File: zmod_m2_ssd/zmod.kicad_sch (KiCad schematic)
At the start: 22 parts, among them J1 MDT420M02001, J2 QTH-020-01-X-D-DP-A, U1 SN74LVC1T45DBV, U2 LTC6957xMS-2, X1 ECS-2520MVQ-1000-BN-TR

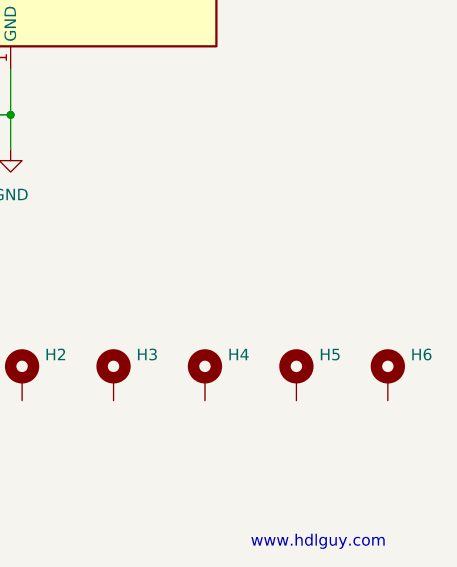
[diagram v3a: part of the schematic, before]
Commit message: added mounting hole for M.2 screw
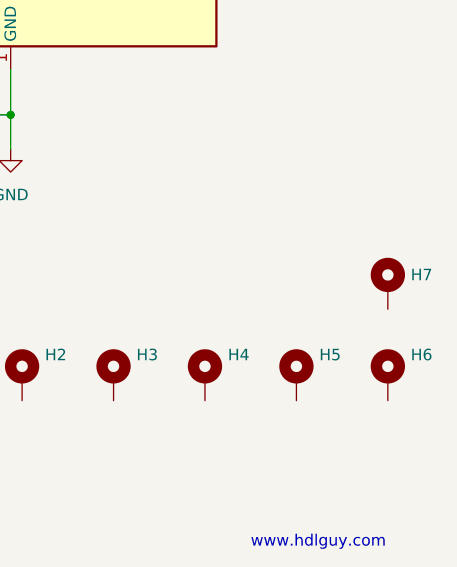
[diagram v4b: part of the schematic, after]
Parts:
- added H7: MountingHole_Pad, MountingHole:MountingHole_2.7mm_Pad, symbol Mechanical:MountingHole_Pad
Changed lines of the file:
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@@
+    (pin "1")
+  )
+  (symbol (lib_id "Mechanical:MountingHole_Pad") (at 279.4 151.13 0) (unit 1)
+    (in_bom yes) (on_board yes) (fields_autoplaced)
+    (property "Reference" "H7" (id 0) (at 281.94 149.8599 0)
+      (effects (font (size 1.27 1.27)) (justify left))
+    )
+    (property "Value" "MountingHole_Pad" (id 1) (at 281.94 151.1299 0)
+      (effects (font (size 1.27 1.27)) (justify left) hide)
+    )
+    (property "Footprint" "MountingHole:MountingHole_2.7mm_Pad" (id 2) (at 279.4 151.13 0)
+      (effects (font (size 1.27 1.27)) hide)
+    )
+    (property "Datasheet" "~" (id 3) (at 279.4 151.13 0)
+      (effects (font (size 1.27 1.27)) hide)
+    )
     (pin "1")
   )
@@
       (reference "H6") (unit 1) (value "MountingHole_Pad") (footprint "MountingHole:MountingHole_3.2mm_M3_DIN965_Pad_TopBottom")
     )
+    (path "/5216a05f-00bb-4954-a8d0-d0c5066122b7"
+      (reference "H7") (unit 1) (value "MountingHole_Pad") (footprint "MountingHole:MountingHole_2.7mm_Pad")
+    )
     (path "/713a8cb6-be5c-413a-968b-156735b7e9f4"

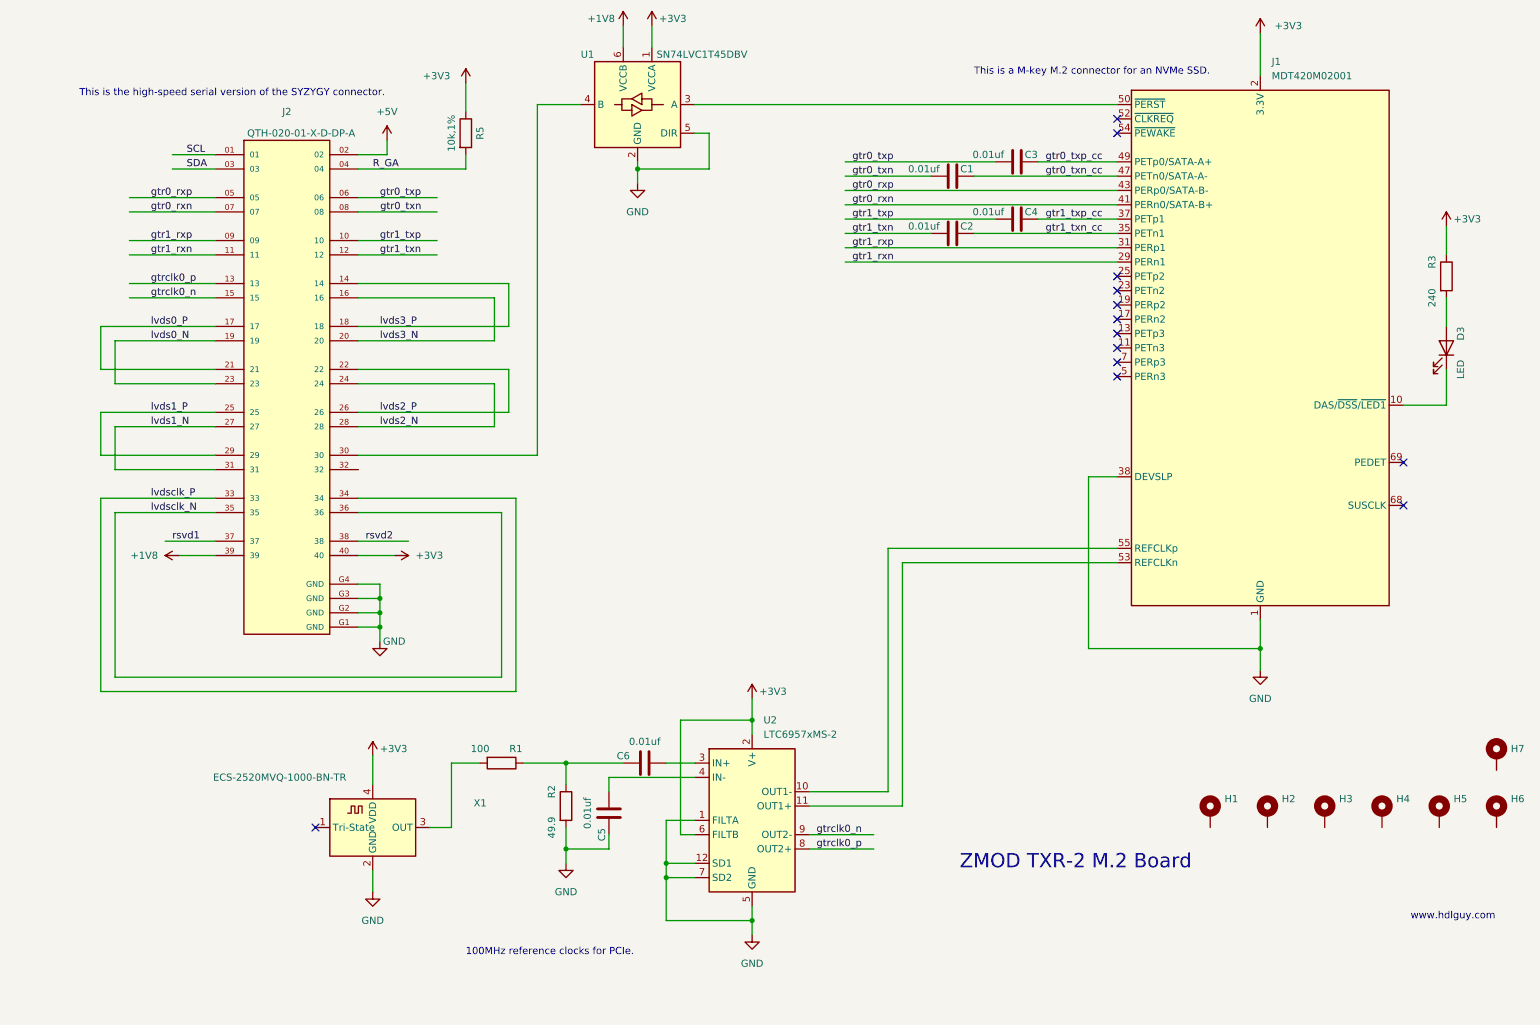
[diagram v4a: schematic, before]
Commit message: first cut at routing the m.2 zmod
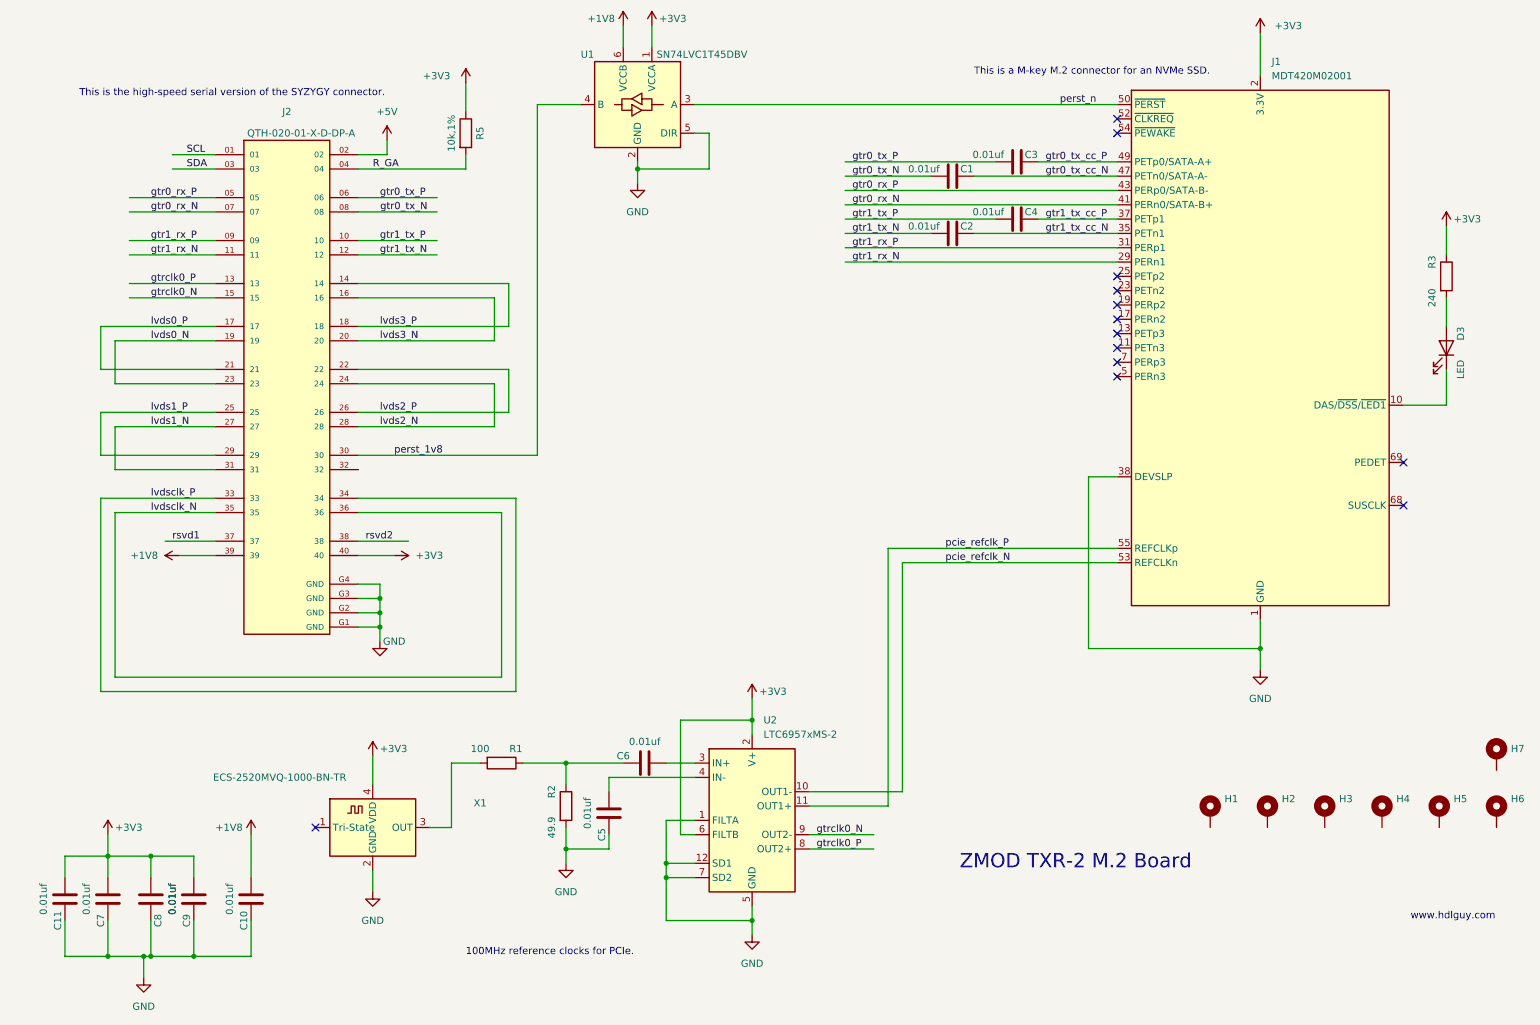
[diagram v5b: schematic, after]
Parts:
- added C10, C11, C7, C8, C9: 0.01uf, Capacitor_SMD:C_0603_1608Metric, symbol Device:C
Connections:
- net +1V8: now also C10.2
- net +3V3: now also C11.2, C7.2, C8.2, C9.2
- net GND: now also C10.1, C11.1, C7.1, C8.1, C9.1
- net perst_1v8: now reaches J2.30, U1.4 (B)
- net perst_n: now reaches J1.50 (~{PERST}), U1.3 (A)
- net pcie_refclk_N: now reaches J1.53 (REFCLKn)
- net pcie_refclk_N: now also U2.10 (OUT1-); no longer U2.11 (OUT1+)
- net pcie_refclk_P: now reaches J1.55 (REFCLKp)
- net pcie_refclk_P: now also U2.11 (OUT1+); no longer U2.10 (OUT1-)
- net gtr0_rxn renamed gtr0_rx_N
- net gtr0_rxp renamed gtr0_rx_P
- net gtr0_txn renamed gtr0_tx_N
- net gtr0_txn_cc renamed gtr0_tx_cc_N
- net gtr0_txp renamed gtr0_tx_P
- net gtr0_txp_cc renamed gtr0_tx_cc_P
- net gtr1_rxn renamed gtr1_rx_N
- net gtr1_rxp renamed gtr1_rx_P
- net gtr1_txn renamed gtr1_tx_N
- net gtr1_txn_cc renamed gtr1_tx_cc_N
- net gtr1_txp renamed gtr1_tx_P
- net gtr1_txp_cc renamed gtr1_tx_cc_P
- net gtrclk0_n renamed gtrclk0_N
- net gtrclk0_p renamed gtrclk0_P

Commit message: ready to send to Oshpark
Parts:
- removed R5: 10k,1%, Resistor_SMD:R_0603_1608Metric, symbol Device:R
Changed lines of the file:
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@@
-    (stroke (width 0) (type default) (color 0 0 0 0))
-  )
-  (wire (pts (xy 96.52 44.45) (xy 96.52 46.99))
     (stroke (width 0) (type default) (color 0 0 0 0))
   )
@@
   )
   (wire (pts (xy 43.18 113.03) (xy 52.07 113.03))
-    (stroke (width 0) (type default) (color 0 0 0 0))
-  )
-  (wire (pts (xy 96.52 31.75) (xy 96.52 36.83))
     (stroke (width 0) (type default) (color 0 0 0 0))
   )
@@
     (pin "1")
     (pin "2")
-  )
-  (symbol (lib_id "power:+3V3") (at 96.52 31.75 0) (unit 1)
-    (in_bom yes) (on_board yes)
-    (property "Reference" "#PWR03" (id 0) (at 96.52 35.56 0)
-      (effects (font (size 1.27 1.27)) hide)
-    )
-    (property "Value" "+3V3" (id 1) (at 88.9 30.48 0)
-      (effects (font (size 1.27 1.27)) (justify left))
-    )
-    (property "Footprint" "" (id 2) (at 96.52 31.75 0)
-      (effects (font (size 1.27 1.27)) hide)
-    )
-    (property "Datasheet" "" (id 3) (at 96.52 31.75 0)
-      (effects (font (size 1.27 1.27)) hide)
-    )
-    (pin "1")
   )
   (symbol (lib_id "Device:R") (at 270.51 66.04 0) (unit 1)
@@
     (pin "2")
   )
-  (symbol (lib_id "Device:R") (at 96.52 40.64 0) (unit 1)
-    (in_bom yes) (on_board yes)
-    (property "Reference" "R5" (id 0) (at 99.06 40.64 90))
-    (property "Value" "10k,1%" (id 1) (at 93.98 40.64 90))
-    (property "Footprint" "Resistor_SMD:R_0603_1608Metric" (id 2) (at 94.742 40.64 90)
-      (effects (font (size 1.27 1.27)) hide)
-    )
-    (property "Datasheet" "~" (id 3) (at 96.52 40.64 0)
-      (effects (font (size 1.27 1.27)) hide)
-    )
-    (pin "1")
-    (pin "2")
-  )
   (symbol (lib_id "Device:C") (at 194.31 45.72 90) (unit 1)
     (in_bom yes) (on_board yes)
@@
       (reference "#PWR02") (unit 1) (value "+5V") (footprint "")
     )
-    (path "/31cfe908-0bdc-41ed-bcd3-98cd266b0e0c"
-      (reference "#PWR03") (unit 1) (value "+3V3") (footprint "")
-    )
     (path "/bc364ec4-e3bc-4253-a49e-0029f83e8206"
       (reference "#PWR04") (unit 1) (value "+3V3") (footprint "")
@@
       (reference "R3") (unit 1) (value "240") (footprint "Resistor_SMD:R_0603_1608Metric")
     )
-    (path "/dfac8798-32e6-44ce-82d4-45466d68831c"
-      (reference "R5") (unit 1) (value "10k,1%") (footprint "Resistor_SMD:R_0603_1608Metric")
-    )
     (path "/87fac8eb-3e82-4d31-b181-231059959fd9"

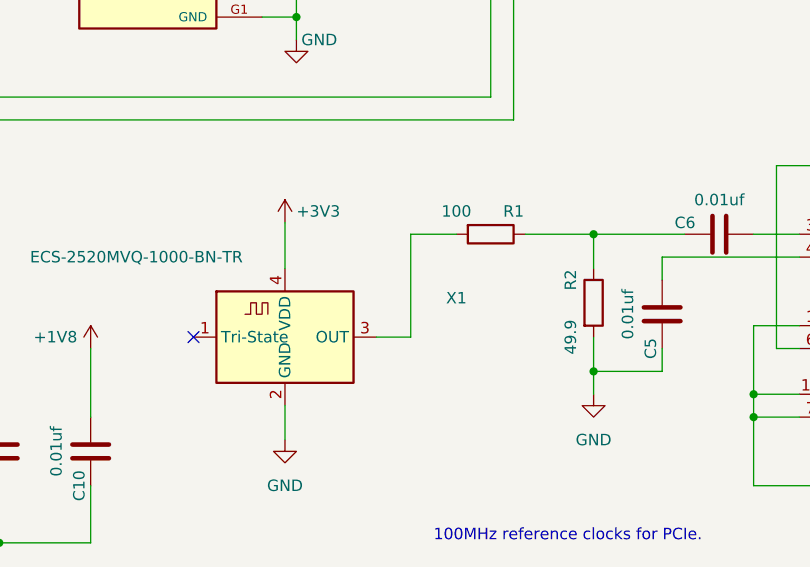
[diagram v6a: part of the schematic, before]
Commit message: updated oscilltor symbol and footprint to have 3D model
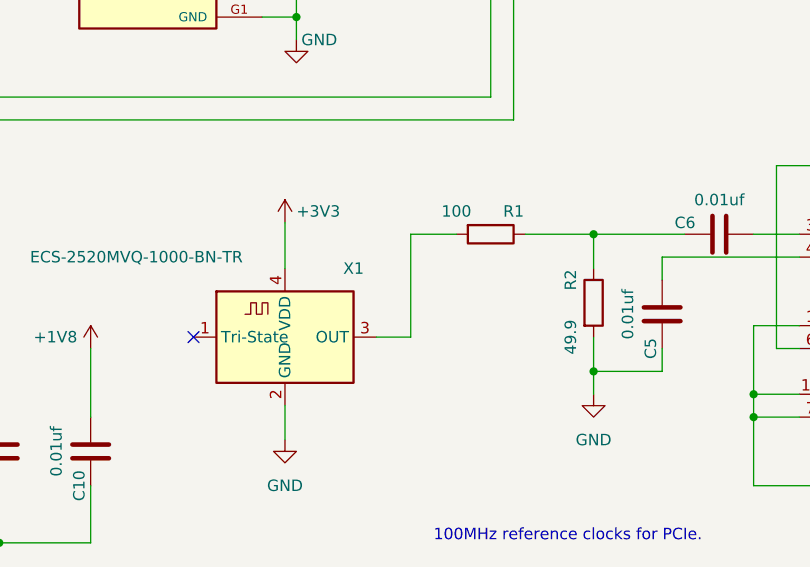
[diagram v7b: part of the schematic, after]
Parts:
- X1: footprint Oscillator:Oscillator_SMD_ECS_2520MV-xxx-xx-4Pin_2.5x2.0mm -> pedrolib:OSC_ECS-2520S25-250-FN-TR; symbol Oscillator:ECS-2520MV-xxx-xx -> pedrolib:ECS-2520MV-xxx-xx
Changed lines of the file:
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@@
     (pin "1")
   )
-  (symbol (lib_id "Oscillator:ECS-2520MV-xxx-xx") (at 80.01 163.83 0) (unit 1)
-    (in_bom yes) (on_board yes)
-    (property "Reference" "X1" (id 0) (at 99.06 159.4993 0))
+  (symbol (lib_id "pedrolib:ECS-2520MV-xxx-xx") (at 80.01 163.83 0) (unit 1)
+    (in_bom yes) (on_board yes)
+    (property "Reference" "X1" (id 0) (at 87.63 156.21 0))
     (property "Value" "ECS-2520MVQ-1000-BN-TR" (id 1) (at 63.5 154.94 0))
-    (property "Footprint" "Oscillator:Oscillator_SMD_ECS_2520MV-xxx-xx-4Pin_2.5x2.0mm" (id 2) (at 91.44 172.72 0)
+    (property "Footprint" "pedrolib:OSC_ECS-2520S25-250-FN-TR" (id 2) (at 91.44 172.72 0)
       (effects (font (size 1.27 1.27)) hide)
     )
@@
     )
     (path "/7c512e96-8c27-4e61-97e0-2f602c82f7f4"
-      (reference "X1") (unit 1) (value "ECS-2520MVQ-1000-BN-TR") (footprint "Oscillator:Oscillator_SMD_ECS_2520MV-xxx-xx-4Pin_2.5x2.0mm")
-    )
-  )
+      (reference "X1") (unit 1) (value "ECS-2520MVQ-1000-BN-TR") (footprint "pedrolib:OSC_ECS-2520S25-250-FN-TR")
+    )
+  )
